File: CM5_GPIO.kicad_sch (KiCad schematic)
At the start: 26 parts, among them J14 JST_SHBM04B-SRSS-TB, J2 Conn_02x07_Odd_Even, J3 Conn_01x03, J7 Micro_SD_Card_Det, J8 THD-20-R, J9 THD-02-R, SW1 Right angle Tact button, U1 TPD4EUSB30, U18 RT9742GGJ5, U2 TPD4EUSB30, U3 MagJack-A70-112-331N126, U5 74LVC1G07SE-7

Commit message: complete first pass at schematic
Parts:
- added J13: THD-02-R, Connector_PinHeader_2.54mm:PinHeader_2x02_P2.54mm_Vertical, symbol Connector_Generic:Conn_02x02_Odd_Even
- added R11, R13: 1k, Resistor_SMD:R_0402_1005Metric, symbol Device:R
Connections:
- net +3.3v: now also J13.1 (Pin_1), J13.2 (Pin_2)
- net at R10.2, U5.4: now also R11.1
- net LED_nACT: now reaches Module1.21 (LED_nACT), R1.2
- net LED_nACT: now also R13.1
- new net: J13.4 (Pin_4), R11.2
- new net: J13.3 (Pin_3), R13.2
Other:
- note added: "Front panel IO"
- moved on the sheet: D1, R10, TP5, U5

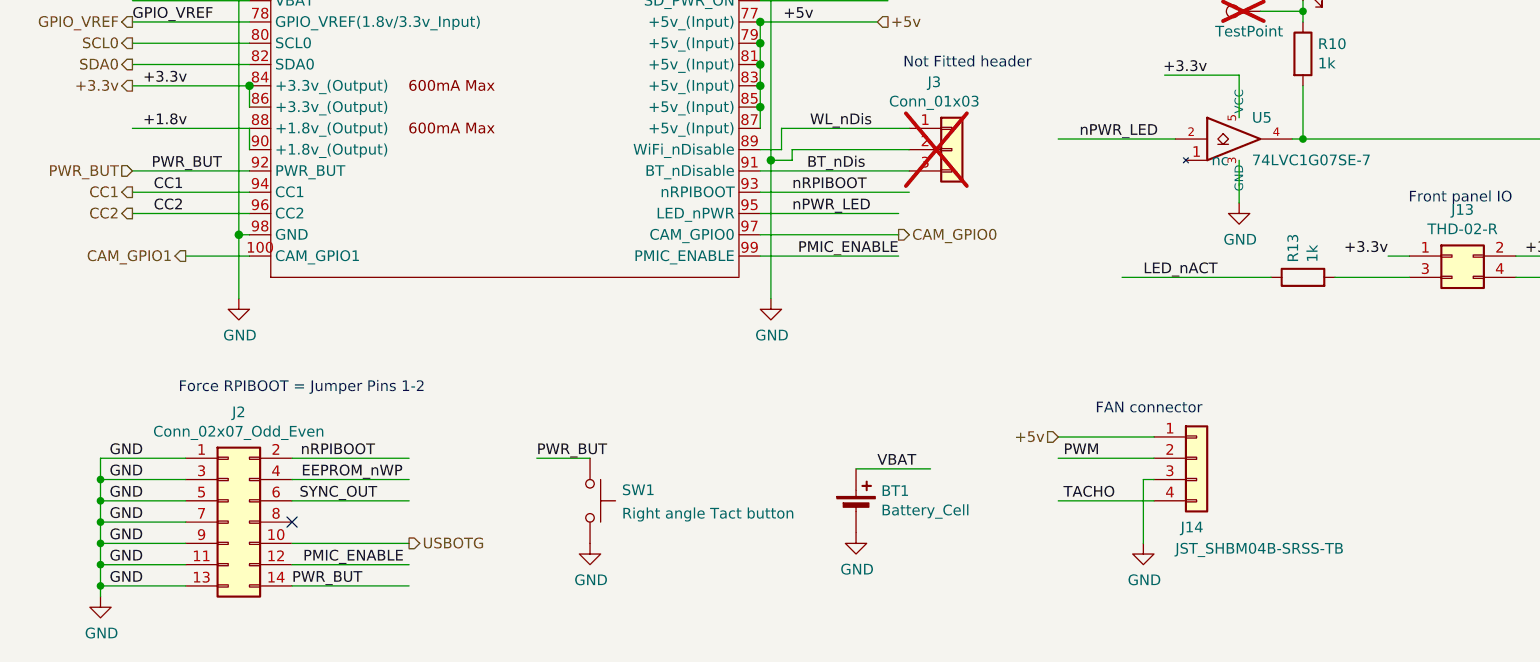
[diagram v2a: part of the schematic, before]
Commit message: add LCSC part numbers, redo fan header and ps_on logic
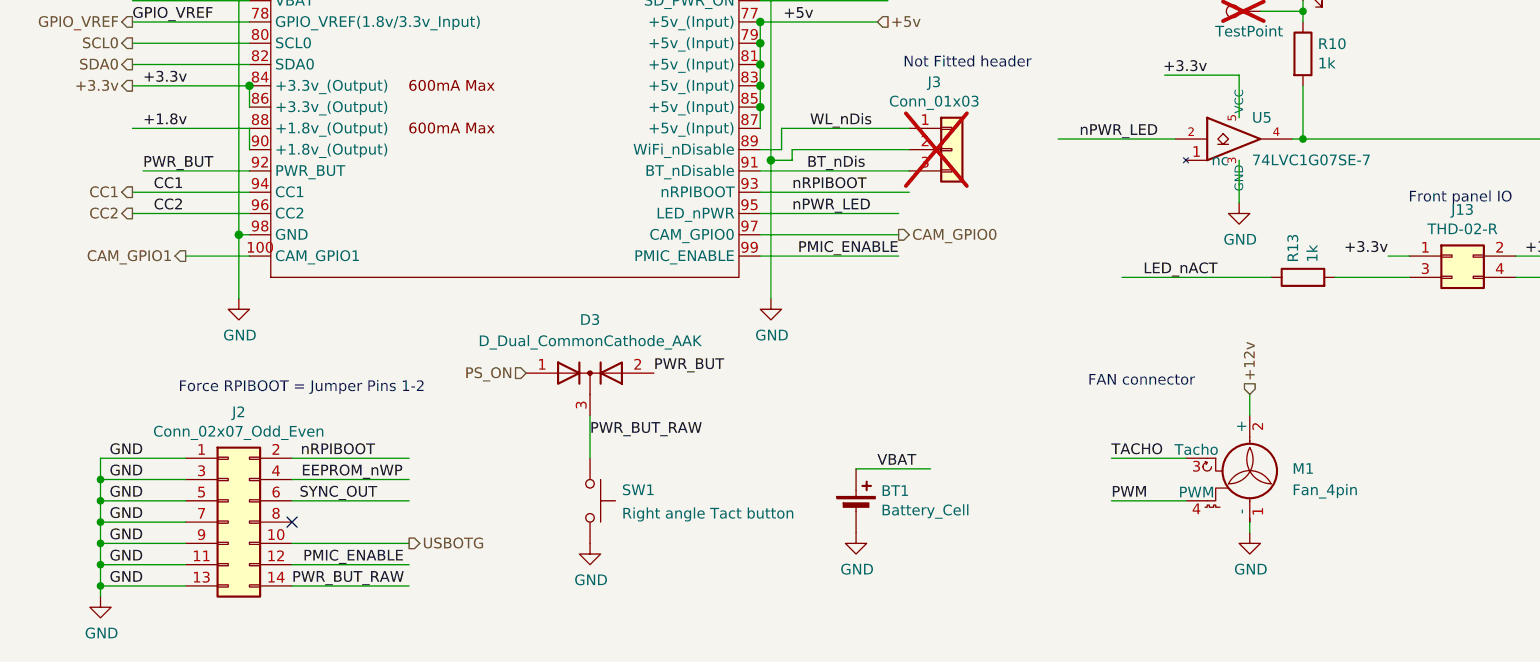
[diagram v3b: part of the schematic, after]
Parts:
- removed J14: JST_SHBM04B-SRSS-TB, Connector_JST:JST_SH_BM04B-SRSS-TB_1x04-1MP_P1.00mm_Vertical, symbol Connector_Generic:Conn_01x04
- added D3: D_Dual_CommonCathode_AAK, Package_TO_SOT_SMD:SOT-23, symbol Device:D_Dual_CommonCathode_AAK
- added M1: Fan_4pin, Connector:FanPinHeader_1x04_P2.54mm_Vertical, symbol Motor:Fan_4pin
- BT1: LCSC (none) -> C5213768
- C1: LCSC (none) -> C92753
- C5: LCSC (none) -> C117956
- D1: LCSC (none) -> C125114
- D2: LCSC (none) -> C125113
- J13, J9: LCSC (none) -> C492419
- J2: LCSC (none) -> C492424
- J7: LCSC (none) -> C428492
- J8: LCSC (none) -> C124383
- Module1: LCSC (none) -> C19089295
- R1, R10, R11, R13: LCSC (none) -> C131360
- R2, R3: LCSC (none) -> C352415
- R5: LCSC (none) -> C17477
- SW1: LCSC (none) -> C127680
- U1, U2: LCSC (none) -> C913227
- U18: LCSC (none) -> C250547
- U5: LCSC (none) -> C67531
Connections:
- net GND: now also M1.1 (-)
- net PWM: now also M1.4 (PWM)
- net PWR_BUT: now also D3.2 (A); no longer J2.14 (Pin_14), SW1.1
- net TACHO: now also M1.3 (Tacho)
- new net +12v: M1.2 (+)
- new net PS_ON: D3.1 (A)
- new net PWR_BUT_RAW: D3.3 (K), J2.14 (Pin_14), SW1.1

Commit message: update PCB
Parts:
- removed C5: 10u, Capacitor_SMD:C_0805_2012Metric, symbol Device:C
- removed J7: Micro_SD_Card_Det, CM5IO:SDCARD_MOLEX_503398-1892, symbol Connector:Micro_SD_Card_Det2
- removed J9: THD-02-R, Connector_PinHeader_2.54mm:PinHeader_2x02_P2.54mm_Vertical, symbol Connector_Generic:Conn_02x02_Odd_Even
- removed U18: RT9742GGJ5, Package_TO_SOT_SMD:SOT-23-5, symbol CM5IO:RT9742GGJ5
- added M2: Fan_4pin, Connector:FanPinHeader_1x04_P2.54mm_Vertical, symbol Motor:Fan_4pin
- SW1: footprint Button_Switch_THT:SW_Tactile_SPST_Angled_PTS645Vx58-2LFS -> Button_Switch_THT:SW_PUSH_6mm
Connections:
- net +12v: now also M2.2 (+)
- net GND: now also M2.1 (-)
- net PWM: now also M2.4 (PWM)
- no-connect marks 9 -> 7
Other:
- note added: "POE removed since POE HATs can't supply 12V"
- note added: "SD card removed because it only works with Lite variants"
- note removed: "CM5Lite SDCARD I/F"
- note removed: "POE Header"
- moved on the sheet: BT1, M1

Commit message: update drop in replacements
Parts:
- D1: mpn (none) -> 150060RS75000
- D2: mpn (none) -> 150060GS75000
- D3: mpn BAT54-05 -> BAT54C
- J13, J8: mpn (none) -> 61304021121
- J2: mpn (none) -> 61301421121
- SW1: mpn (none) -> 430186050716
- U5: mpn (none) -> 74LVC1G07GW

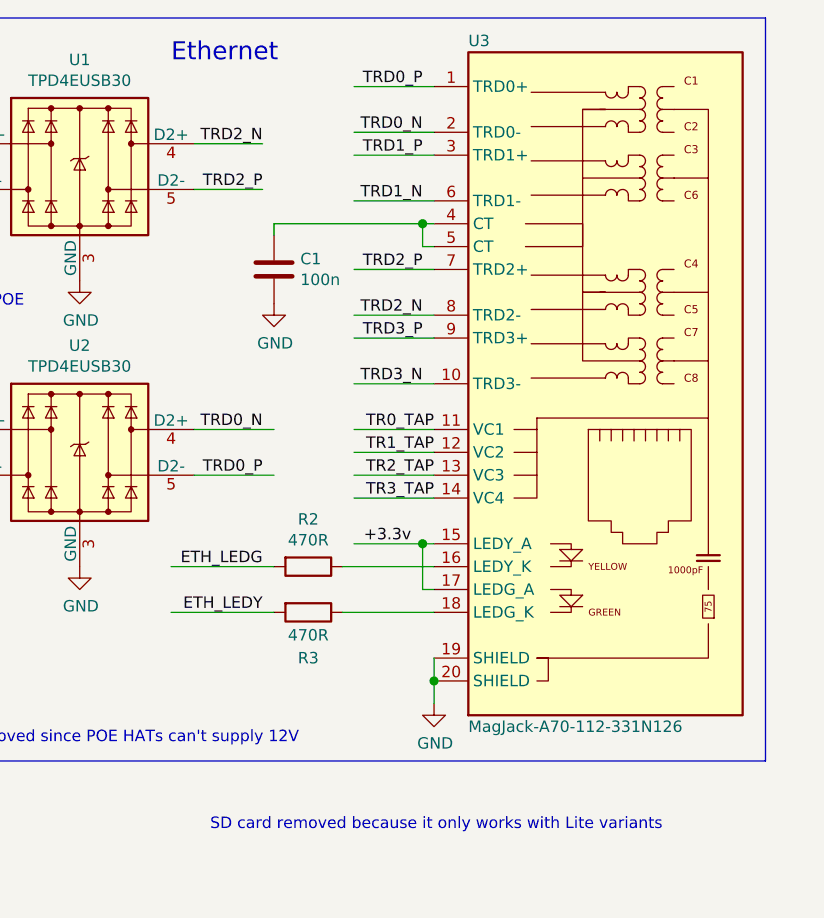
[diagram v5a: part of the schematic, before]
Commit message: update ethernet connector
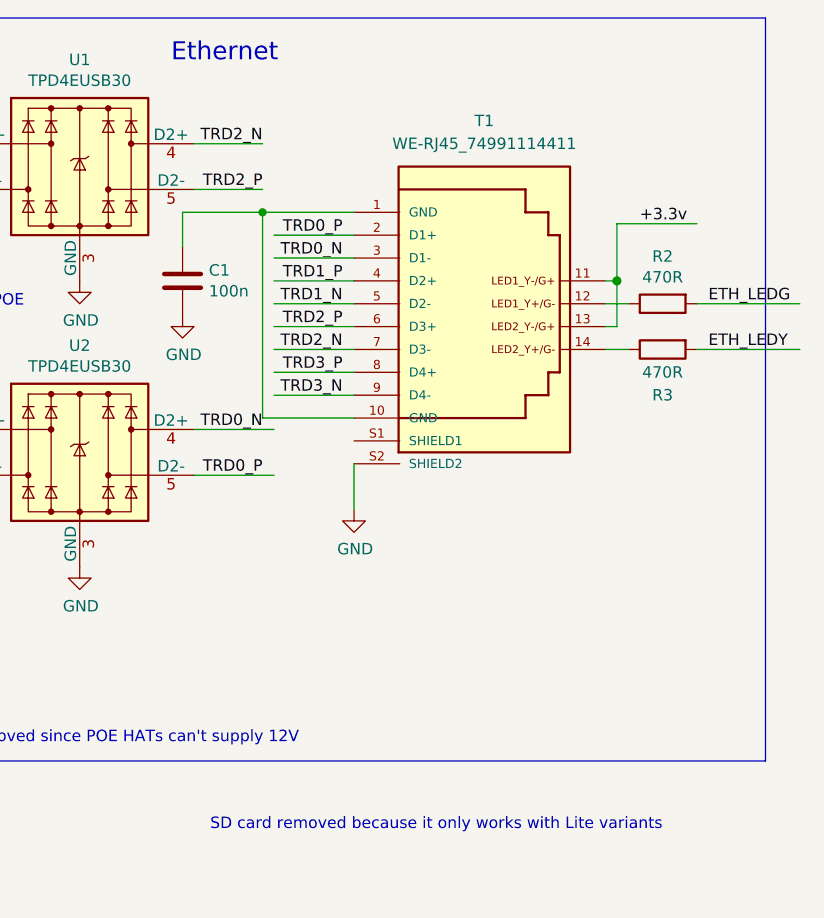
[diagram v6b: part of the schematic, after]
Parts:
- removed U3: MagJack-A70-112-331N126, CM5IO:TRJG0926HENL, symbol CM5IO:MagJack-A70-112-331N126
- added T1: WE-RJ45_74991114411, CM5IO:74991114411, symbol CM5IO:WE-RJ45_74991114411
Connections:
- net +3.3v: now also T1.11, T1.13
- net GND: now also T1.S2 (SHIELD2)
- net TRD0_N: now also T1.3 (D1-)
- net TRD0_P: now also T1.2 (D1+)
- net TRD1_N: now also T1.5 (D2-)
- net TRD1_P: now also T1.4 (D2+)
- net TRD2_N: now also T1.7 (D3-)
- net TRD2_P: now also T1.6 (D3+)
- net TRD3_N: now also T1.9 (D4-)
- net TRD3_P: now also T1.8 (D4+)
- net at C1.1: now also T1.1 (GND), T1.10 (GND)
- net at R2.1: now also T1.12
- net at R3.1: now also T1.14
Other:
- moved on the sheet: C1, R2, R3

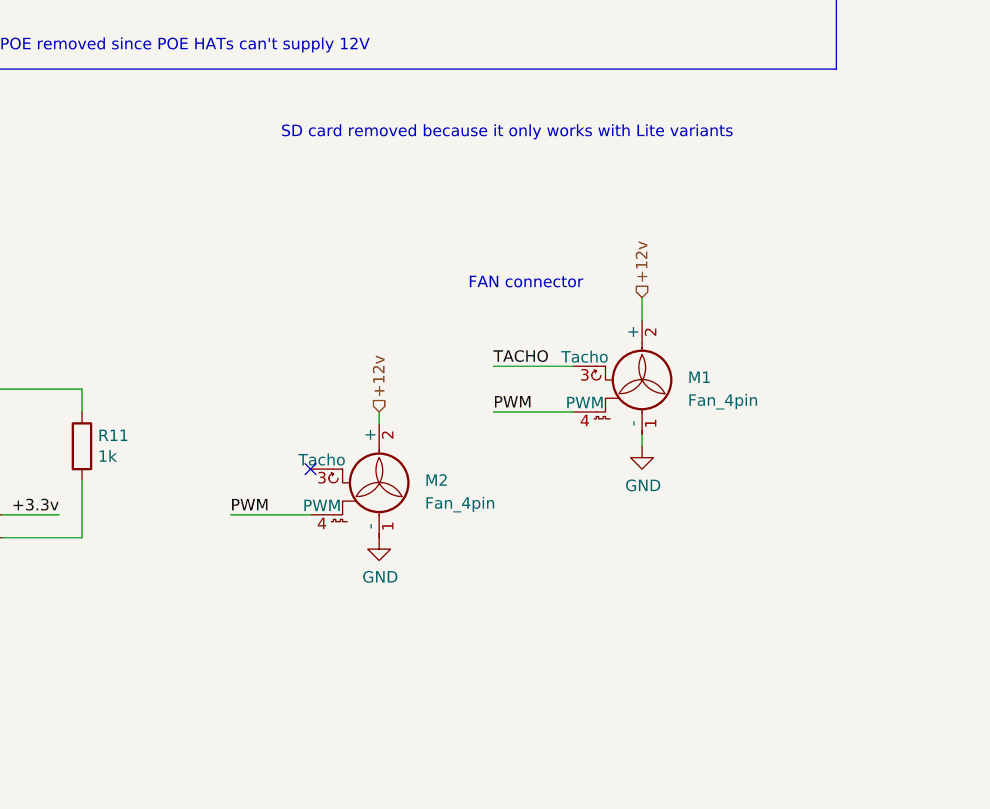
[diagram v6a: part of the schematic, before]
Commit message: add fan protection
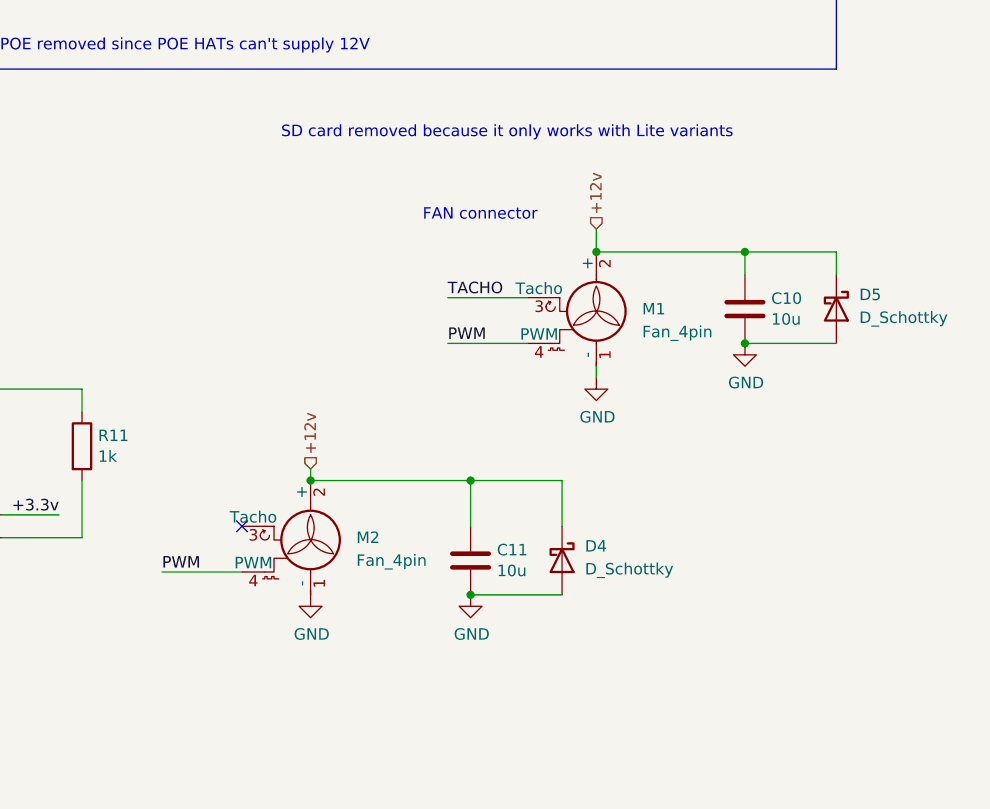
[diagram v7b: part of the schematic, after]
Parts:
- added C10, C11: 10u, Capacitor_SMD:C_0805_2012Metric, symbol Device:C
- added D4, D5: D_Schottky, Diode_SMD:D_SMA, symbol Device:D_Schottky
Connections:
- net +12v: now also C10.1, C11.1, D4.1 (K), D5.1 (K)
- net GND: now also C10.2, C11.2, D4.2 (A), D5.2 (A)
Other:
- moved on the sheet: M1, M2

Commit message: more aisler changes
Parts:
- Module1: mpn (none) -> 10164227-1001A1RLF
- T1: mpn (none) -> 74991114411
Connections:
- net GND: now also T1.S1 (SHIELD1)
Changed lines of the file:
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@@
 	)
 	(junction
+		(at 237.49 63.5)
+		(diameter 0)
+		(color 0 0 0 0)
+	)
+	(junction
 		(at 101.6 95.25)
 		(diameter 1.016)
@@
 	(wire
 		(pts
+			(xy 237.49 60.96) (xy 237.49 63.5)
+		)
+		(stroke
+			(width 0)
+			(type default)
+		)
+	)
+	(wire
+		(pts
 			(xy 44.45 172.72) (xy 58.42 172.72)
 		)
@@
 			)
 		)
+		(property "mpn" "10164227-1001A1RLF"
+			(at 72.39 77.47 0)
+			(effects
+				(font
+					(size 1.27 1.27)
+				)
+				(hide yes)
+			)
+		)
 		(pin "1"
 		)
@@
 				(hide yes)
 			)
+		)
+		(property "mpn" "74991114411"
+			(at 250.19 45.72 0)
+			(effects
+				(font
+					(size 1.27 1.27)
+				)
+				(hide yes)
+			)
